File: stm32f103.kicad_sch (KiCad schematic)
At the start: 50 parts, among them J1 12Vin, J2 SYSTEM_BOOT_JUMP, J3 ADC_PIN, J4 BOOTLOADER_UART, J5 MY_BOOT_JUMP, J6 ARM_JTAG, SW1 RESET, U1 MC33063AD, U2 STM32F103RETx, U3 AMS1117-3.3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

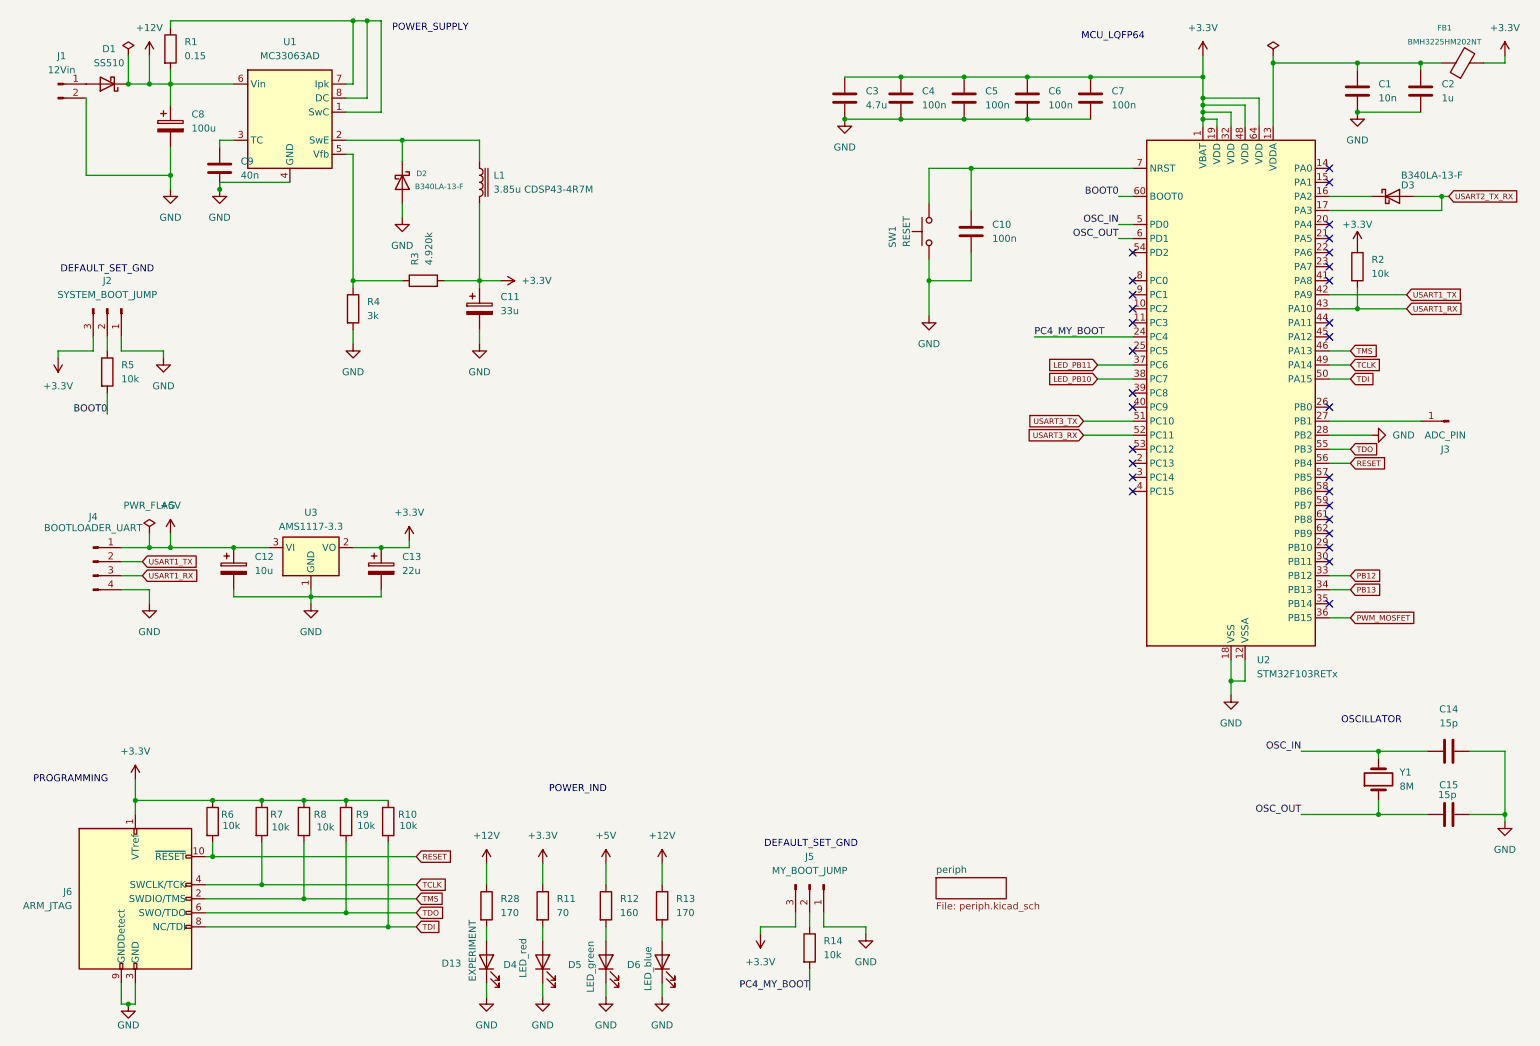
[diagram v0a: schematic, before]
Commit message: Some rearrangements have been made in schematics
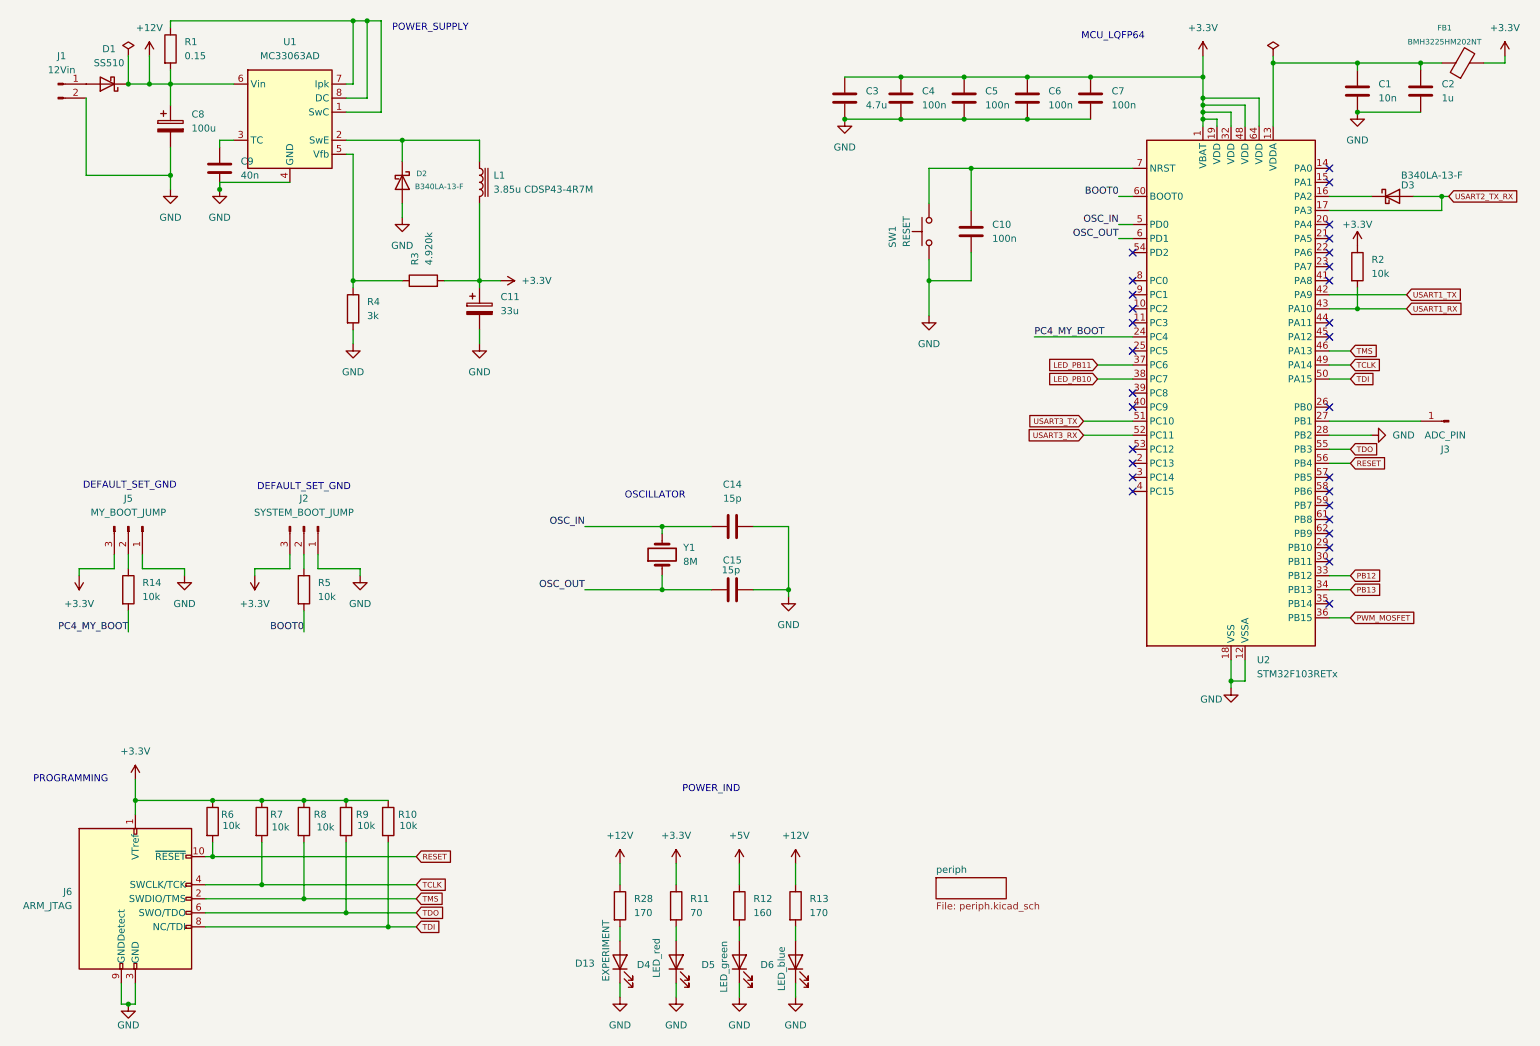
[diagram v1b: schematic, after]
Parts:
- removed C12: 10u, Capacitor_Tantalum_SMD:CP_EIA-3216-12_Kemet-S_HandSolder, symbol Device:C_Polarized
- removed C13: 22u, Capacitor_Tantalum_SMD:CP_EIA-3216-12_Kemet-S_HandSolder, symbol Device:C_Polarized
- removed J4: BOOTLOADER_UART, Connector:NS-Tech_Grove_1x04_P2mm_Vertical, symbol Connector:Conn_01x04_Pin
- removed U3: AMS1117-3.3, Package_TO_SOT_SMD:SOT-223-3_TabPin2, symbol Regulator_Linear:AMS1117-3.3
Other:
- moved on the sheet: C14, C15, D13, D4, D5, D6, J2, J5, R11, R12, R13, R14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

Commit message: Frames in schematics has been added. Types of mounting holes has been replaced
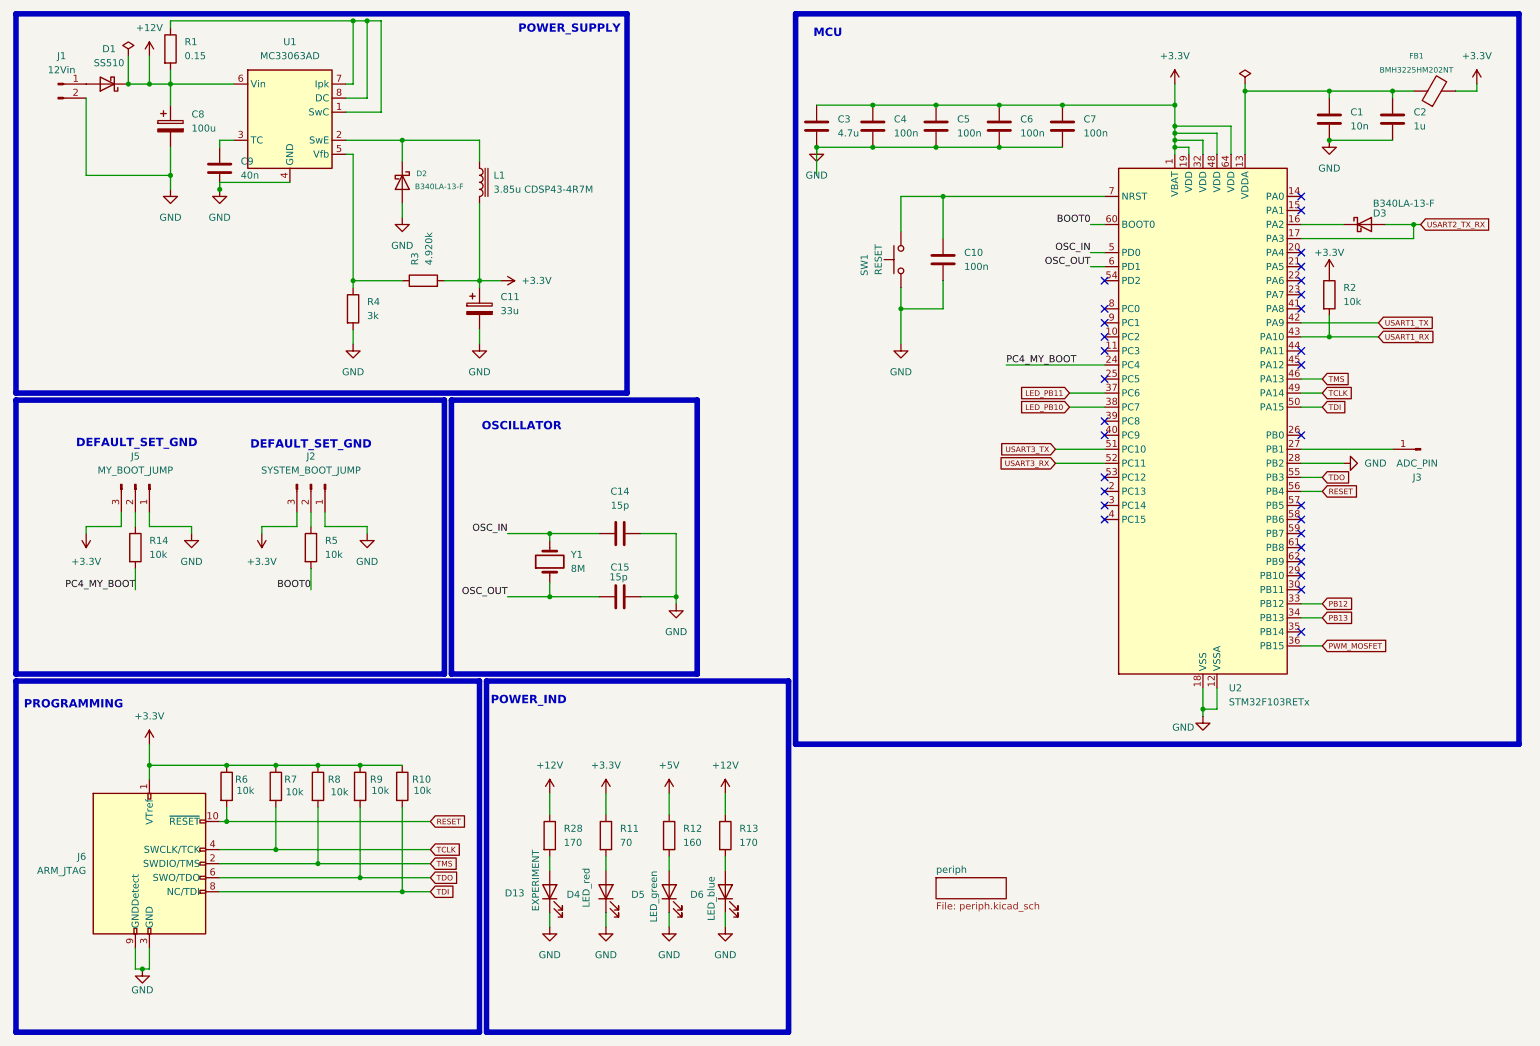
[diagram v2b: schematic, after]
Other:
- note added: "MCU"
- note removed: "MCU_LQFP64"
- moved on the sheet: C1, C10, C14, C15, C2, C3, C4, C5, C6, C7, D13, D3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

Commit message: Comments have been added to the schemas
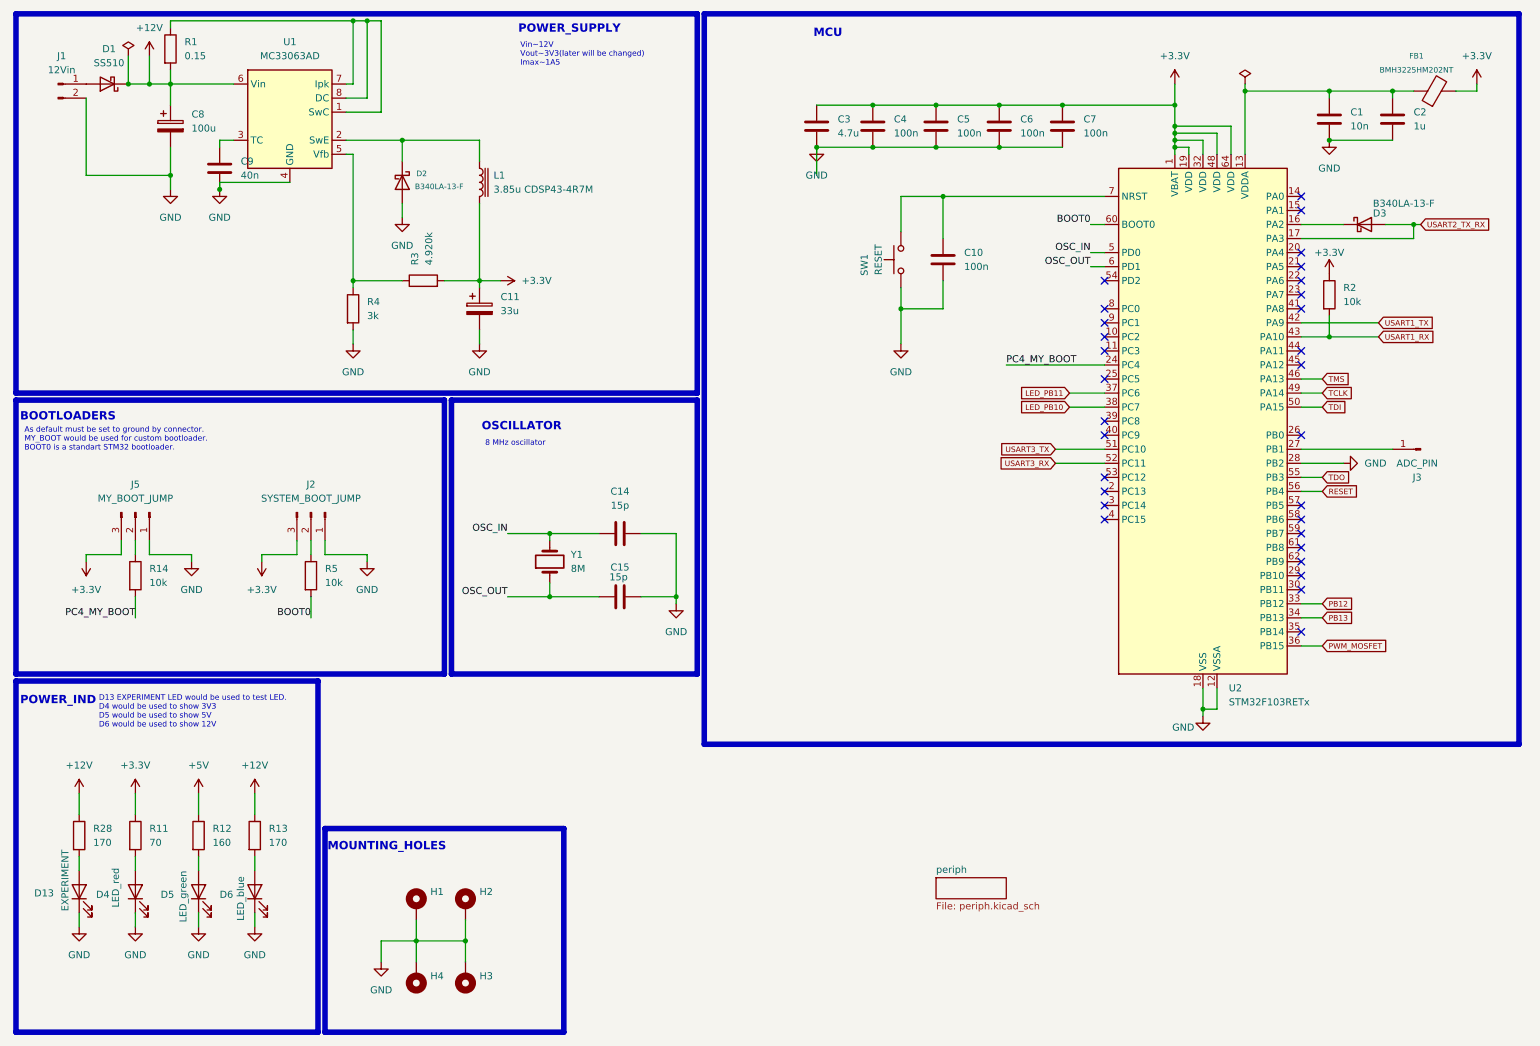
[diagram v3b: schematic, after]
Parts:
- removed J6: ARM_JTAG, Connector_PinHeader_1.27mm:PinHeader_2x05_P1.27mm_Vertical, symbol Connector:Conn_ARM_JTAG_SWD_10
- removed R10, R6, R7, R8, R9: 10k, Resistor_SMD:R_1206_3216Metric_Pad1.30x1.75mm_HandSolder, symbol Device:R
- added H1, H2, H3, H4: MountingHole_Pad, MountingHole:MountingHole_3.2mm_M3_Pad_Via, symbol Mechanical:MountingHole_Pad
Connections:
- net GND: now also H1.1, H2.1, H3.1, H4.1
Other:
- note added: "8 MHz oscillator"
- note added: "As default must be set to ground by connector. MY_BOOT would be used for custom bootloader. BOOT0 is a standart STM32 bootloader."
- note added: "BOOTLOADERS"
- note added: "D13 EXPERIMENT LED would be used to test LED. D4 would be used to show 3V3 D5 would be used to show 5V D6 would be used to show 12V"
- note added: "MOUNTING_HOLES"
- note added: "Vin~12V Vout~3V3(later will be changed) Imax~1A5"
- note removed: "DEFAULT_SET_GND"
- note removed: "PROGRAMMING"
- moved on the sheet: D13, D4, D5, D6, J2, J5, R11, R12, R13, R14, R28, R5

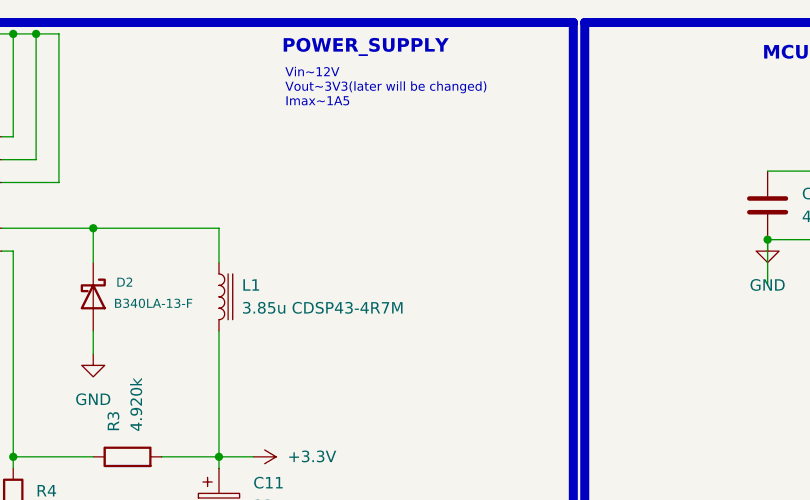
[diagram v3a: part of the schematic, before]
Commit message: Images of schema has been added and some components value has been changed@
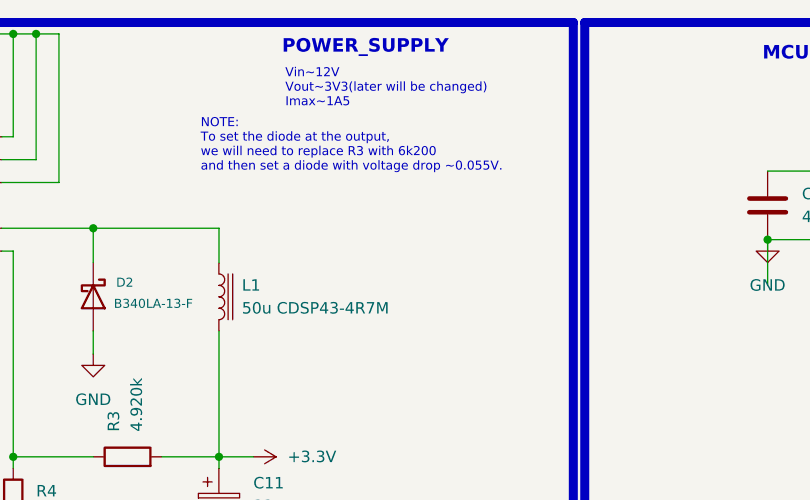
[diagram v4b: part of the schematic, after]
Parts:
- L1: value 3.85u CDSP43-4R7M -> 50u CDSP43-4R7M
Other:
- note added: "NOTE: To set the diode at the output, we will need to replace R3 with 6k200 and then set a diode with voltage drop ~0.055V."
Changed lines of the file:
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@@
 		)
 	)
+	(text "NOTE:\nTo set the diode at the output, \nwe will need to replace R3 with 6k200\nand then set a diode with voltage drop ~0.055V.\n"
+		(exclude_from_sim no)
+		(at 94.488 26.416 0)
+		(effects
+			(font
+				(size 1 1)
+				(thickness 0.125)
+				(color 0 0 0 1)
+			)
+			(justify left)
+		)
+	)
 	(text "OSCILLATOR"
 		(exclude_from_sim no)
@@
 			)
 		)
-		(property "Value" "3.85u CDSP43-4R7M"
+		(property "Value" "50u CDSP43-4R7M"
 			(at 99.06 44.4499 0)
 			(effects

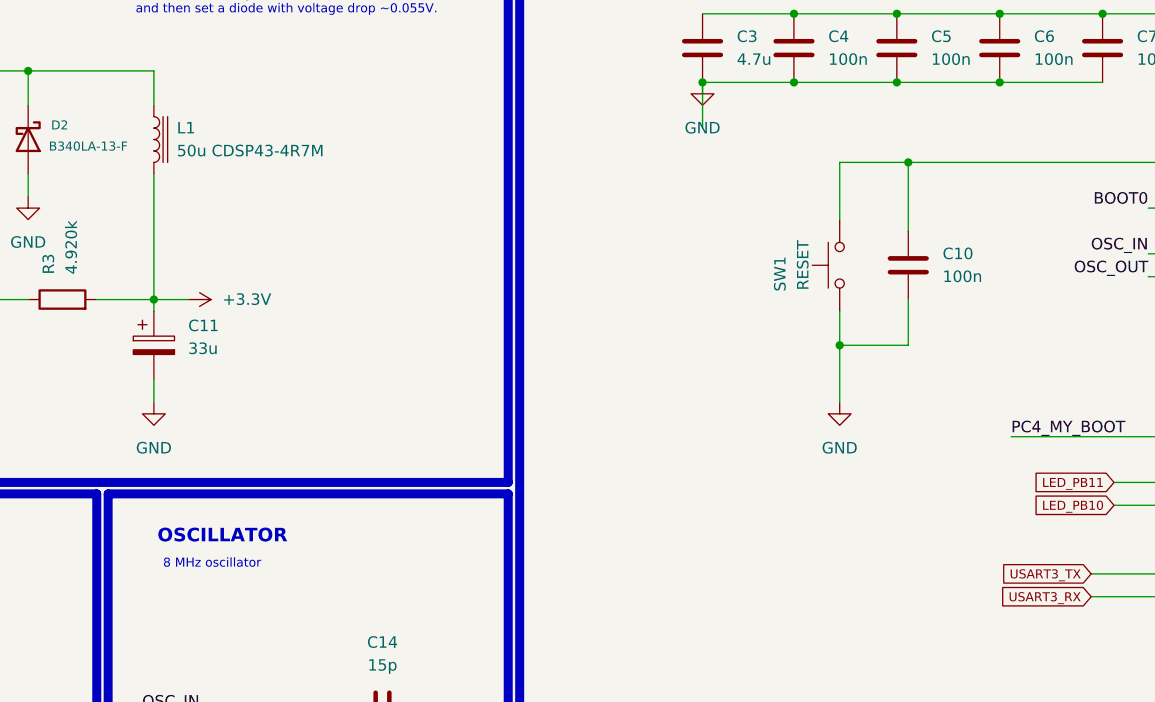
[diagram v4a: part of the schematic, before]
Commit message: Footprints of bootloaders and boots have been changed also has been cahnged ADC pin header, reset LED have been added, and diode for switch
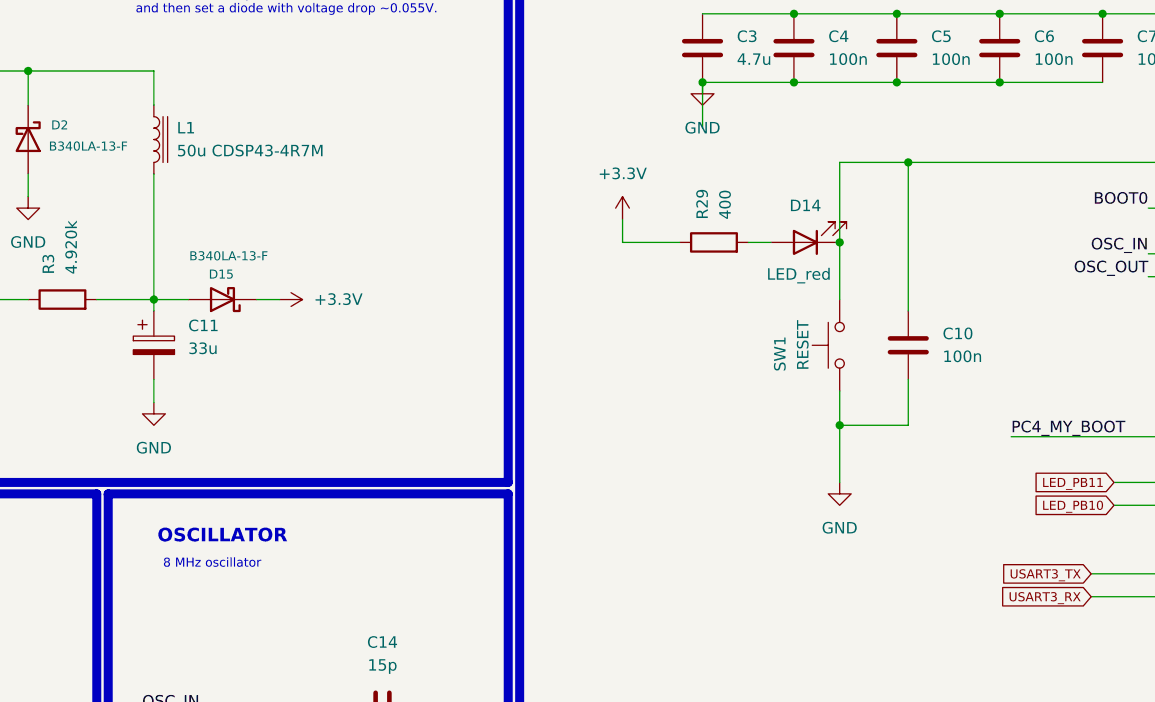
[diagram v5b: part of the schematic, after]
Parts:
- added D14: LED_red, LED_SMD:LED_1206_3216Metric_Pad1.42x1.75mm_HandSolder, symbol Device:LED
- added D15: B340LA-13-F, Diode_SMD:D_SMA_Handsoldering, symbol Diode:1N5822
- added R29: 400, Resistor_SMD:R_1206_3216Metric_Pad1.30x1.75mm_HandSolder, symbol Device:R
- J2, J5: footprint Connector_PinHeader_1.00mm:PinHeader_1x03_P1.00mm_Vertical -> Connector_PinHeader_2.54mm:PinHeader_1x03_P2.54mm_Vertical
- J3: footprint Connector_PinHeader_1.00mm:PinHeader_1x01_P1.00mm_Vertical -> Connector_PinHeader_2.54mm:PinHeader_1x01_P2.54mm_Vertical
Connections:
- net +3.3V: now also D15.1 (K), R29.1; no longer C11.1, L1.2, R3.2
- net at C10.1, SW1.2, U2.7 (NRST): now also D14.1 (K)
- new net: D14.2 (A), R29.2
- new net: C11.1, D15.2 (A), L1.2, R3.2
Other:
- moved on the sheet: C10, SW1
